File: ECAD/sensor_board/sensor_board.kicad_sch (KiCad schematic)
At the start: 32 parts, among them J1 Conn_01x02, J2 Conn_01x04, J3 Conn_01x02, Q2 Q_PMOS_GSD, Q3 Q_PMOS_GSD, Q4 2N7002, SW2 SW_SPST, U1 TPL5111, U2 TPS22917DBV, U3 TC2030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

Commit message: Pushing updates to schematic
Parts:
- removed H3: MountingHole, MountingHole:MountingHole_8.4mm_M8, symbol Mechanical:MountingHole
- removed SW2: SW_SPST, symbol Switch:SW_SPST
- added H3, H4: M3, MountingHole:MountingHole_3.2mm_M3_Pad, symbol Mechanical:MountingHole_Pad
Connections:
- net GND: now also H3.1, H4.1
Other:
- note added: "TODO Now: - Coincell holder for CR2025: -- Use 3034TR from Keystone -- Add JLC part # - Connectors J1, J3: -- Make pads -- Add JLC part # - Add footprints for J2, U3 (Alex has footprints) - Review mounting hole sizes and update mechanical enclosure as needed"
- note removed: "TODO: - Coincell holder for CR2025 - Add connectors: J1, J3 - Review and remove grounded and ungrounded mounting holes: H1, H2, H3"

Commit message: Format and adding footprints
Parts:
- removed J1, J3: Conn_01x02, BLE_Scale_V1:JST_SH_SM02B-SRSS-TB_1x02-1MP_P1.00mm_Horizontal, symbol Connector_Generic:Conn_01x02
- added BT1: CR2025, symbol Device:Battery_Cell
- added J4: S4B-XH-SM4-TB, FloMon:S4B-XH-SM4-TB, symbol Connector_Generic:Conn_01x04
- added JP2: ~, Jumper:SolderJumper-2_P1.3mm_Bridged_RoundedPad1.0x1.5mm, symbol Jumper:SolderJumper_2_Bridged
- added R4: 330k, Resistor_SMD:R_0603_1608Metric, symbol Device:R_US
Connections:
- net +BATT: now also J4.1 (Pin_1), J4.3 (Pin_3)
- net FLOW_SENSE: now also J4.2 (Pin_2), J4.4 (Pin_4), JP2.2 (B), R4.1; no longer R2.1, R9.1, U1.3 (DELAY/M_DRV)
- net GND: now also BT1.2 (-), R4.2
- net at D1.2 (A2), J2.2 (Pin_2), JP1.2 (B)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: now also BT1.1 (+)
- new net: JP2.1 (A), R2.1, R9.1, U1.3 (DELAY/M_DRV)
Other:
- note removed: "Flow Sensor Input"
- title: (none) -> FM-001A FloMon Sensor Module
- moved on the sheet: C1, C10, C11, C2, C3, C9, D1, H1, H2, H3, H4, J2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

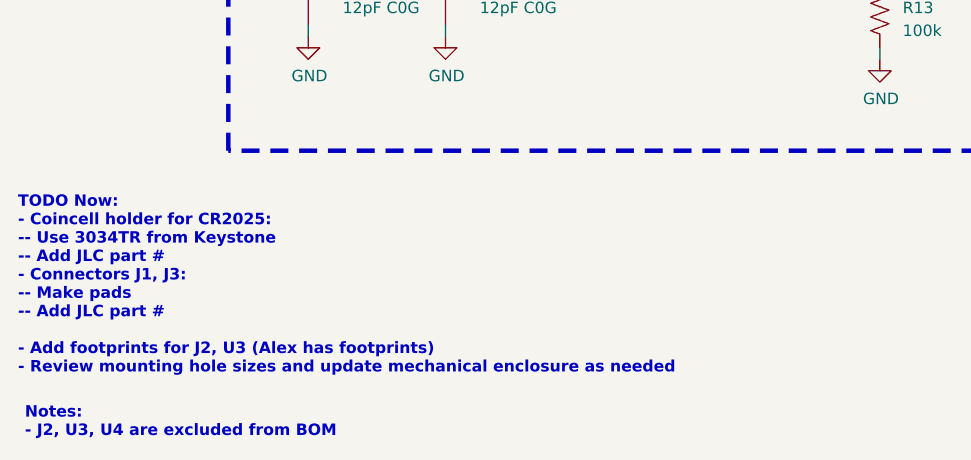
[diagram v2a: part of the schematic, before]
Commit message: PCB Editor updates: updated settings (e.g. Design Rules under Board Setup), added footprints to library, added parts to PCB
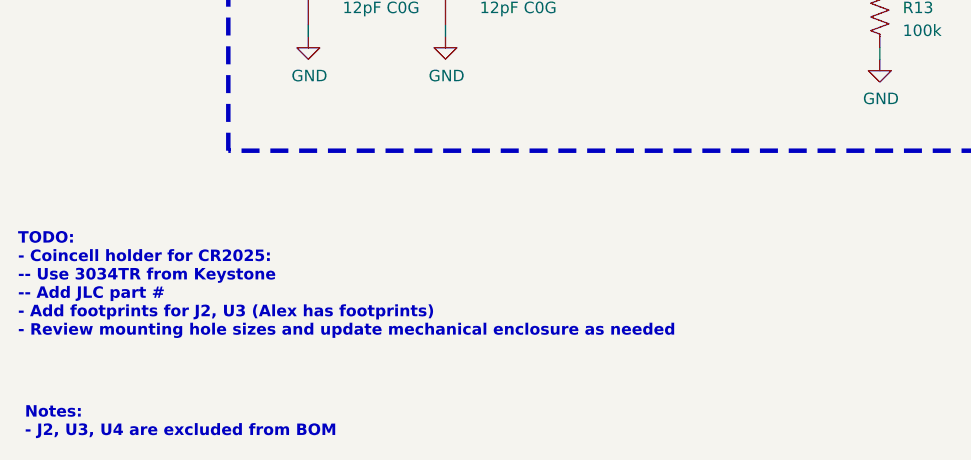
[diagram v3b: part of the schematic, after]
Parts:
- J2: footprint BLE_Scale_V1:Test_Wire_Pad_x4 -> FloMon:Test_Wire_Pad_x4
- U3: footprint BLE_Scale_V1:TC2030-IDC-NL -> FloMon:TC2030-IDC-NL
- U4: footprint BLE_Scale_V1:BC805M_No_Paste -> FloMon:BC805M_No_Paste
- Y1: footprint BLE_Scale_V1:Crystal_SMD_3215-2Pin_3.2x1.5mm -> FloMon:Crystal_SMD_3215-2Pin_3.2x1.5mm
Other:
- note added: "TODO: - Coincell holder for CR2025: -- Use 3034TR from Keystone -- Add JLC part # - Add footprints for J2, U3 (Alex has footprints) - Review mounting hole sizes and update mechanical enclosure as needed"
- note removed: "TODO Now: - Coincell holder for CR2025: -- Use 3034TR from Keystone -- Add JLC part # - Connectors J1, J3: -- Make pads -- Add JLC part # - Add footprints for J2, U3 (Alex has footprints) - Review mounting hole sizes and update mechanical enclosure as needed"
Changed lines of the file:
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@@
 		)
 	)
-	(text "TODO Now:\n- Coincell holder for CR2025:\n-- Use 3034TR from Keystone\n-- Add JLC part #\n- Connectors J1, J3:\n-- Make pads\n-- Add JLC part #\n\n- Add footprints for J2, U3 (Alex has footprints)\n- Review mounting hole sizes and update mechanical enclosure as needed"
+	(text "TODO:\n- Coincell holder for CR2025:\n-- Use 3034TR from Keystone\n-- Add JLC part #\n- Add footprints for J2, U3 (Alex has footprints)\n- Review mounting hole sizes and update mechanical enclosure as needed"
 		(exclude_from_sim no)
 		(at 17.272 246.126 0)
@@
 			)
 		)
-		(property "Footprint" "BLE_Scale_V1:BC805M_No_Paste"
+		(property "Footprint" "FloMon:BC805M_No_Paste"
 			(at 90.17 179.07 0)
 			(effects
@@
 			)
 		)
-		(property "Footprint" "BLE_Scale_V1:Test_Wire_Pad_x4"
+		(property "Footprint" "FloMon:Test_Wire_Pad_x4"
 			(at 73.66 27.94 0)
 			(effects
@@
 			)
 		)
-		(property "Footprint" "BLE_Scale_V1:TC2030-IDC-NL"
+		(property "Footprint" "FloMon:TC2030-IDC-NL"
 			(at 55.88 171.45 0)
 			(effects
@@
 			)
 		)
-		(property "Footprint" "BLE_Scale_V1:Crystal_SMD_3215-2Pin_3.2x1.5mm"
+		(property "Footprint" "FloMon:Crystal_SMD_3215-2Pin_3.2x1.5mm"
 			(at 57.15 207.01 0)
 			(effects
